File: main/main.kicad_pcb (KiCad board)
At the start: 2 copper layers, 45.1 x 52.6 mm, 37 parts, among them P2 CONN_5, P7 CONN_10, P8 CONN_7, U1 MKL03Z32VFK4, U2 IS31FL3737, U4 ESD

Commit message: Make the values of RGB LEDs "RGB LED".
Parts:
- D_LK1, D_RK1, D_TK1: value Val** -> RGB_LED
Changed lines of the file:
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@@
       (effects (font (size 0.75 0.75) (thickness 0.15)) (justify mirror))
     )
-    (fp_text value Val** (at 0.143677 -3.386134) (layer F.SilkS) hide
+    (fp_text value RGB_LED (at 0.143677 -3.386134) (layer F.SilkS) hide
       (effects (font (size 0.75 0.75) (thickness 0.15)))
     )
@@
       (effects (font (size 0.75 0.75) (thickness 0.15)) (justify mirror))
     )
-    (fp_text value Val** (at -0.224715 -7.053988) (layer F.SilkS) hide
+    (fp_text value RGB_LED (at -0.224715 -7.053988) (layer F.SilkS) hide
       (effects (font (size 0.75 0.75) (thickness 0.15)))
     )
@@
       (effects (font (size 0.75 0.75) (thickness 0.15)) (justify mirror))
     )
-    (fp_text value Val** (at -1.787495 -7.551008) (layer F.SilkS) hide
+    (fp_text value RGB_LED (at -1.787495 -7.551008) (layer F.SilkS) hide
       (effects (font (size 0.75 0.75) (thickness 0.15)))
     )

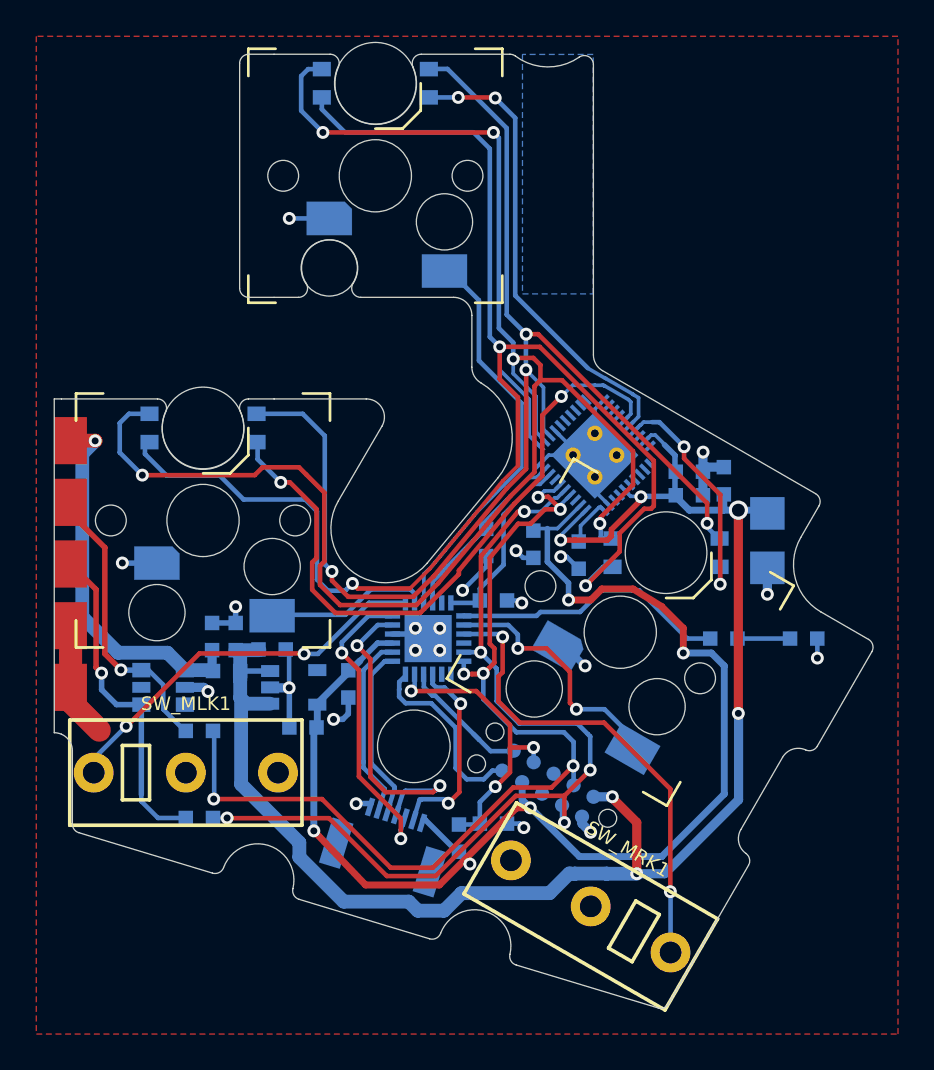
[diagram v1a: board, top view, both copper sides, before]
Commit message: Place tracks farther from the edges.
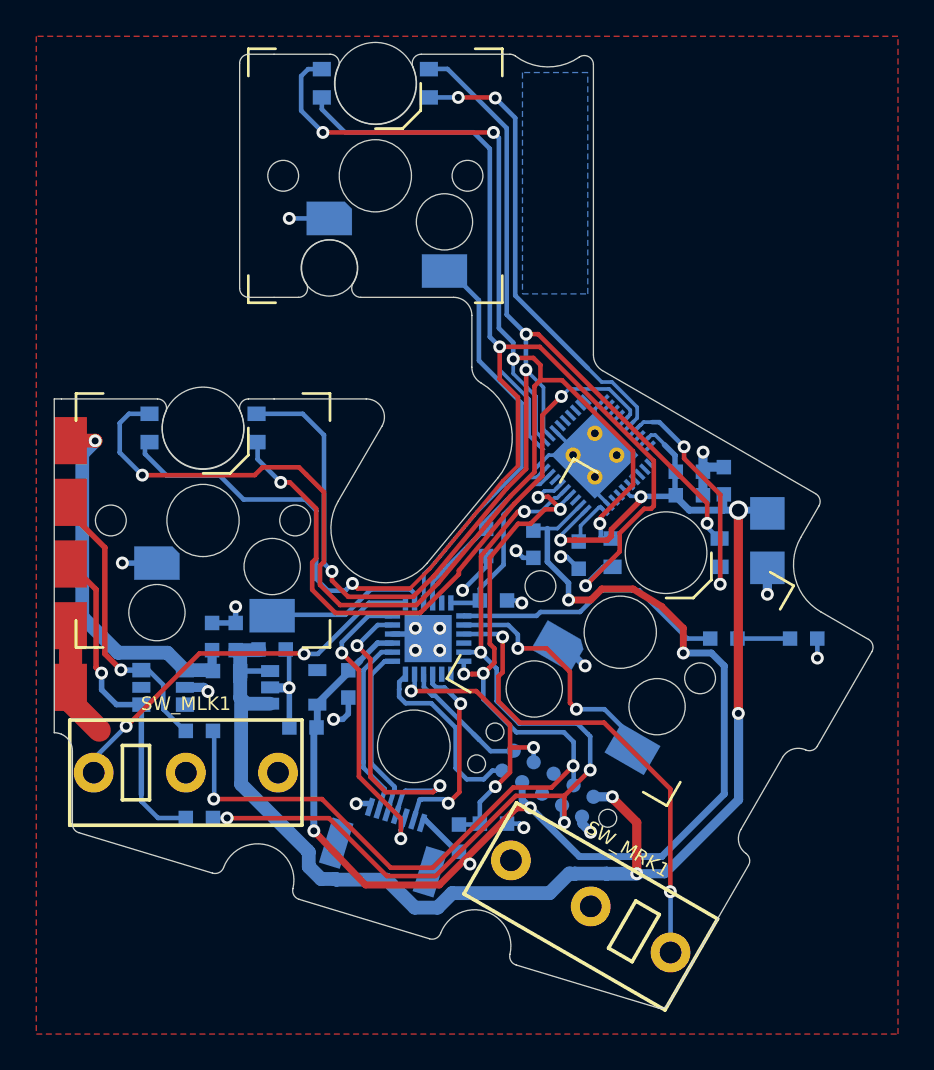
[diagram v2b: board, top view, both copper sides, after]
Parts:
- moved G*** 0.10 mm to (152.6, 88.1)

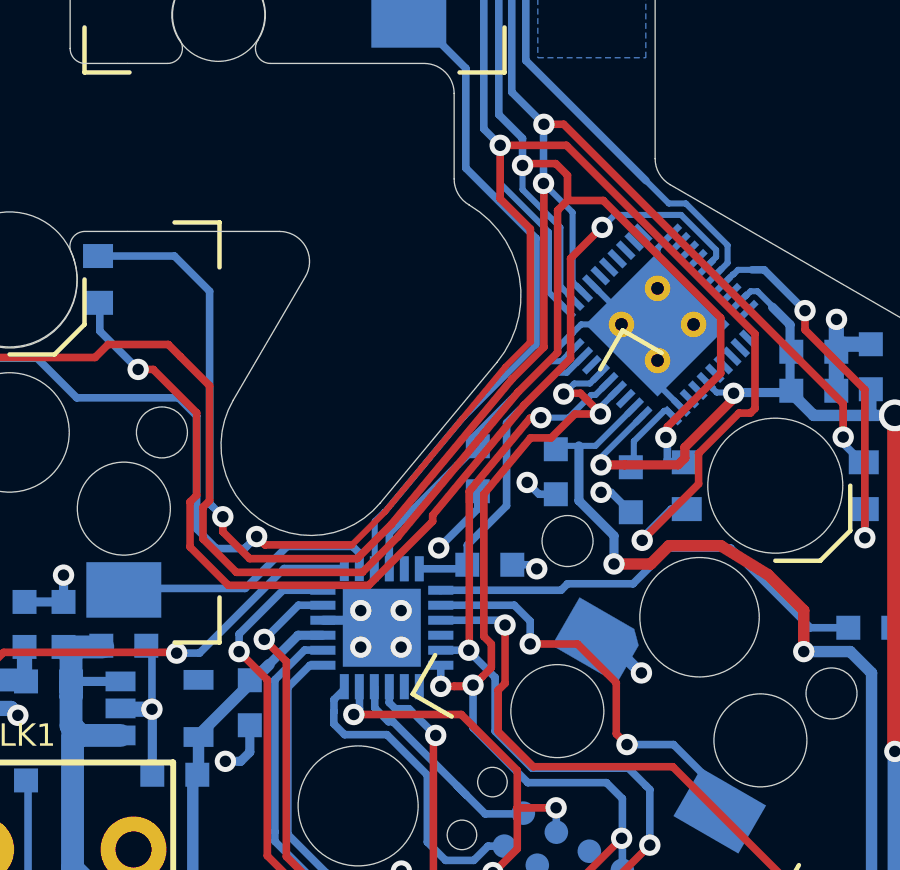
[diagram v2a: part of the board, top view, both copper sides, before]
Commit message: Put copper farther from edges.
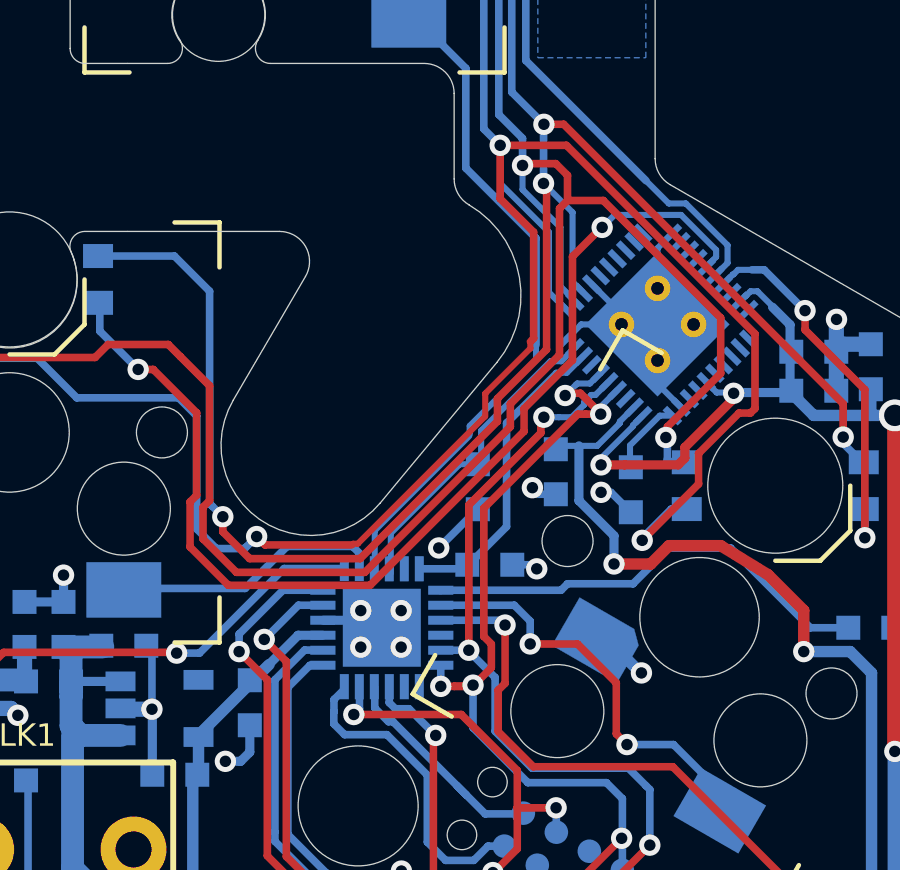
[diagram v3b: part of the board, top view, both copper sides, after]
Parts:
- moved R3 0.60 mm to (148.8, 108.5)
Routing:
- net GND: track 46.9 -> 46.1 mm

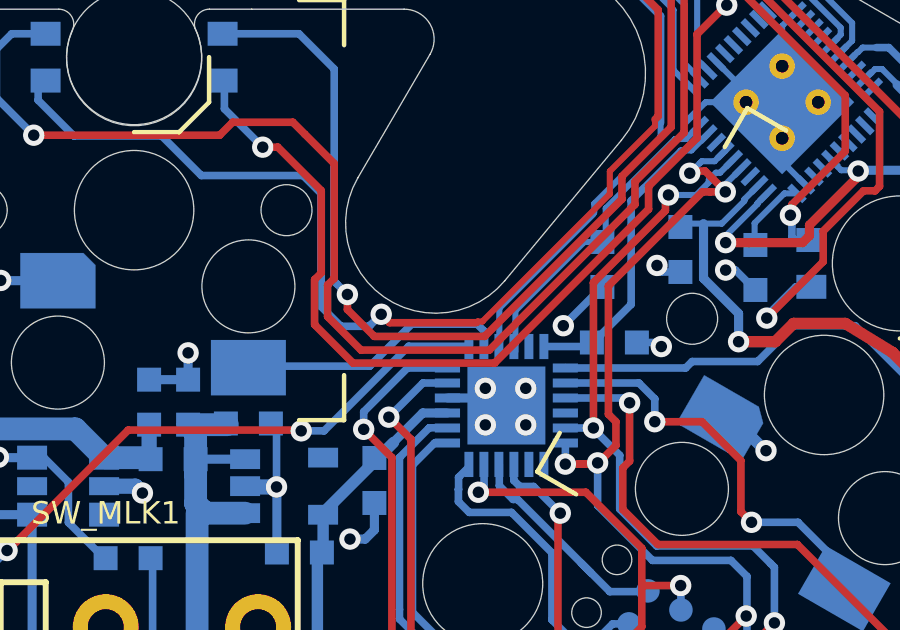
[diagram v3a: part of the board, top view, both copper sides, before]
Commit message: Put copper farther from edges.
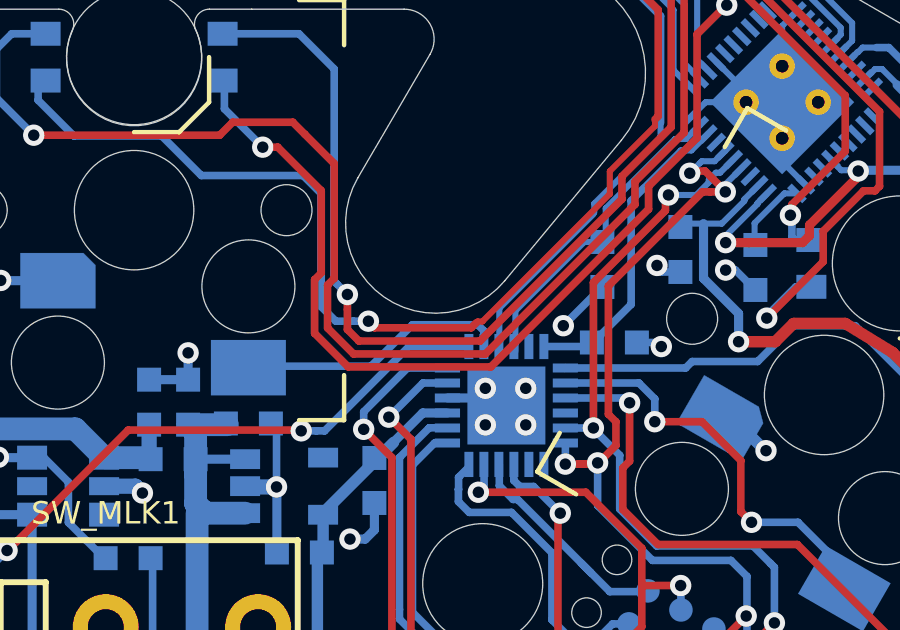
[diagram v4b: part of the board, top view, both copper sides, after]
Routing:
- net /LED_SW3: track 72.2 -> 72.7 mm

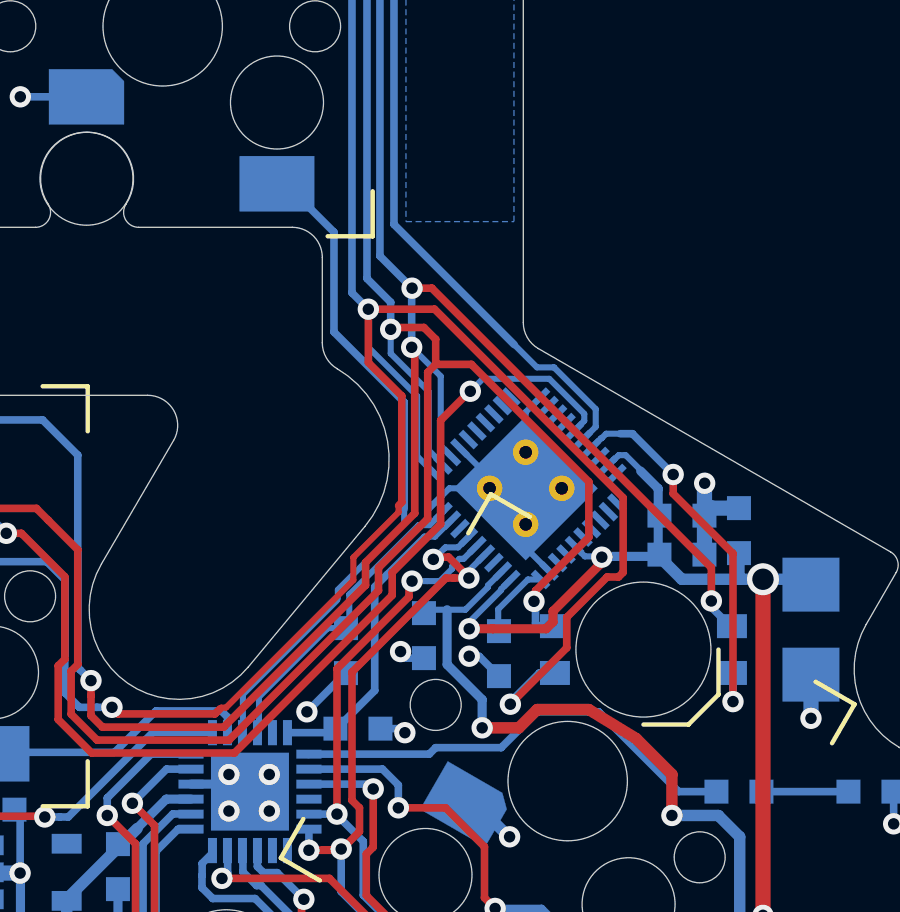
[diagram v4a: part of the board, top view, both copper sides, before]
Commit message: Put copper 0.25+ mm from edges.
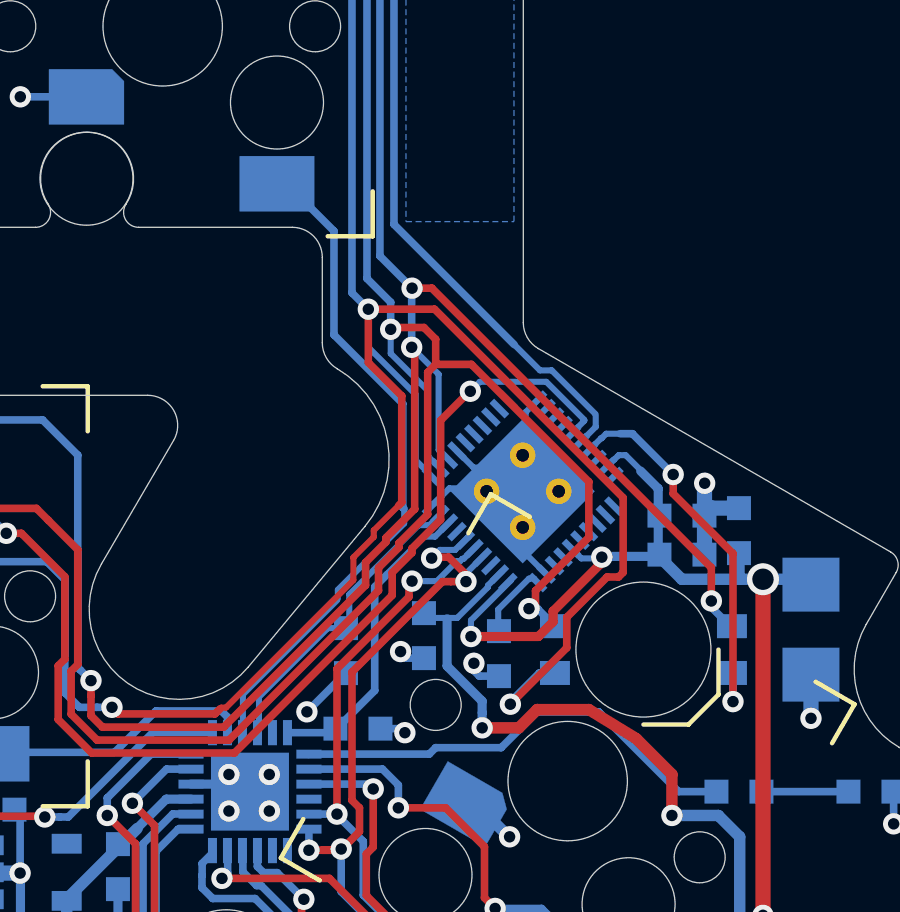
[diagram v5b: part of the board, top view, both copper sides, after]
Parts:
- moved U2 0.14 mm to (154.7, 103.2)
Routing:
- net GND: track 46.1 -> 45.4 mm
